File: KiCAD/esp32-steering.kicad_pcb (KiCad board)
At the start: 2 copper layers, 142 x 142 mm, 26 parts, among them J1 Conn_01x02, SW1 RotaryEncoder_Switch_MP, SW2 RotaryEncoder_Switch_MP, SW4 SW_SPST, SW5 SW_SPST

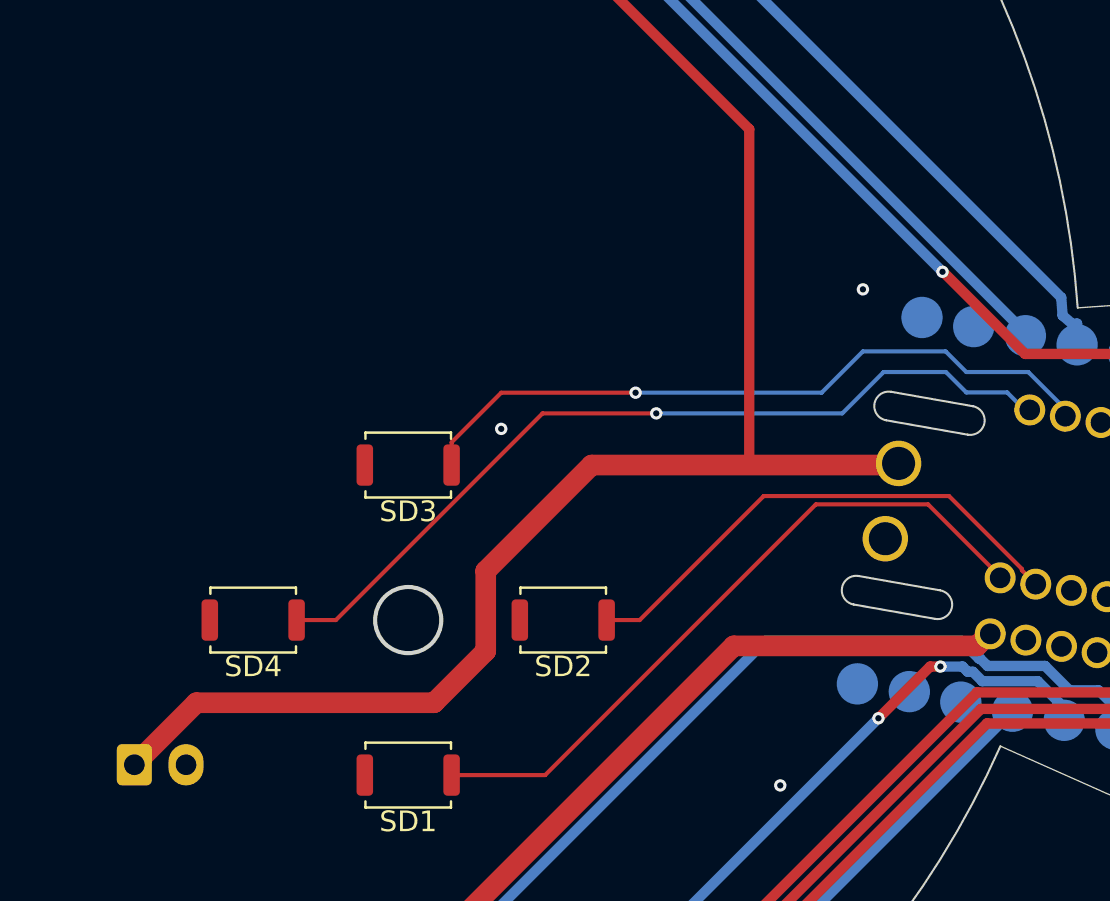
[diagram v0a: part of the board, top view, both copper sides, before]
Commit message: correct footprint and pcb design for battery connections
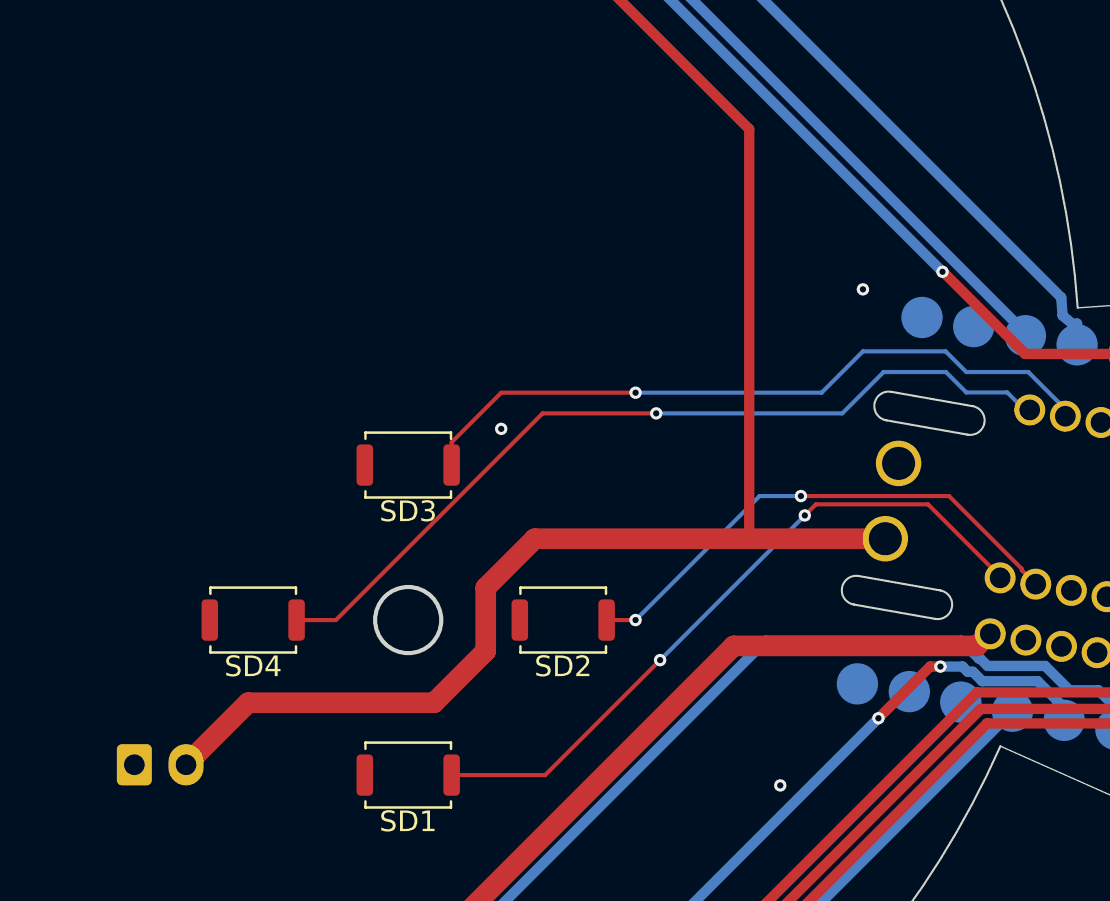
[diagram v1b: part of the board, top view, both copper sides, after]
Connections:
- J1 pad 1: +5V -> GND
- J1 pad 2: GND -> +5V
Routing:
- net +5V: track 169.2 -> 167.6 mm
- net /BUTD2: track 25.1 -> 25.3 mm, vias 0 -> 2
- net /BUTD1: vias 0 -> 2
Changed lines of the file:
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@@
 		(tags "D2FC-F-7N20M ")
 		(property "Reference" "SW5"
-			(at 0.040628 -12.709186 12.223)
+			(at 0.040629 -12.709186 12.223)
 			(unlocked yes)
 			(layer "B.SilkS")
@@
 			(remove_unused_layers no)
 			(roundrect_rratio 0.147059)
-			(net 25 "+5V")
+			(net 2 "GND")
 			(pinfunction "Pin_1")
 			(pintype "passive")
@@
 			(layers "*.Cu" "*.Mask")
 			(remove_unused_layers no)
-			(net 2 "GND")
+			(net 25 "+5V")
 			(pinfunction "Pin_2")
 			(pintype "passive")
@@
 		(fp_poly
 			(pts
-				(xy -4.5 13.25) (xy 4.500001 13.25) (xy 4.5 6.25) (xy -4.5 6.25)
+				(xy -4.5 13.25) (xy 4.500003 13.25) (xy 4.5 6.25) (xy -4.5 6.25)
 			)
 			(stroke
@@
 		(fp_arc
 			(start -5.2 7)
-			(mid -4.5 6.299999)
+			(mid -4.5 6.299998)
 			(end -3.8 7)
 			(stroke
@@
 		)
 		(pad "19" thru_hole circle
-			(at -1.85 10.05 260)
+			(at 1.85 10.05 260)
 			(size 2.2 2.2)
 			(drill 1.6)
@@
 		)
 		(pad "20" thru_hole circle
-			(at 1.85 10.05 260)
+			(at -1.85 10.05 260)
 			(size 2.2 2.2)
 			(drill 1.6)
@@
 	)
 	(segment
+		(start 135.725131 104.420742)
+		(end 135.645873 104.5)
+		(width 1)
+		(layer "F.Cu")
+		(net 2)
+	)
+	(segment
 		(start 160.351906 128.617429)
 		(end 160.351906 130.729669)
@@
 	)
 	(segment
-		(start 75.5 47)
-		(end 98.5 70)
+		(start 65.053238 44.370458)
+		(end 65.053238 47.37816)
 		(width 0.5)
 		(layer "F.Cu")
@@
 	)
 	(segment
-		(start 98.5 70)
-		(end 110.25 70)
+		(start 66.175078 48.5)
+		(end 67.75 48.5)
 		(width 0.5)
 		(layer "F.Cu")
@@
 	)
 	(segment
-		(start 135.725131 104.420742)
-		(end 135.645873 104.5)
-		(width 1)
+		(start 69.25 47)
+		(end 75.5 47)
+		(width 0.5)
 		(layer "F.Cu")
 		(net 25)
@@
 	)
 	(segment
-		(start 67.75 48.5)
-		(end 69.25 47)
+		(start 65.053238 47.37816)
+		(end 66.175078 48.5)
 		(width 0.5)
 		(layer "F.Cu")
@@
 	)
 	(segment
-		(start 135.645873 104.5)
-		(end 120.875 104.5)
-		(width 1)
+		(start 128.5 88.25)
+		(end 128.5 108.06453)
+		(width 0.5)
 		(layer "F.Cu")
 		(net 25)
 	)
 	(segment
-		(start 69.25 47)
-		(end 75.5 47)
+		(start 98.5 70)
+		(end 110.25 70)
 		(width 0.5)
 		(layer "F.Cu")
@@
 	)
 	(segment
+		(start 115.75 113.5)
+		(end 113.25 116)
+		(width 1)
+		(layer "F.Cu")
+		(net 25)
+	)
+	(segment
 		(start 130.703238 41.920458)
 		(end 130.703238 39.615617)
@@
 	)
 	(segment
-		(start 115.75 109.625)
-		(end 115.75 113.5)
+		(start 67.75 48.5)
+		(end 69.25 47)
+		(width 0.5)
+		(layer "F.Cu")
+		(net 25)
+	)
+	(segment
+		(start 118.12297 108.06453)
+		(end 115.75 110.4375)
 		(width 1)
 		(layer "F.Cu")
@@
 	)
 	(segment
-		(start 101.75 116)
-		(end 98.75 119)
-		(width 1)
-		(layer "F.Cu")
-		(net 25)
-	)
-	(segment
 		(start 93.736915 34.603531)
 		(end 93.736915 32.5)
@@
 	)
 	(segment
-		(start 115.75 113.5)
-		(end 113.25 116)
-		(width 1)
-		(layer "F.Cu")
-		(net 25)
-	)
-	(segment
-		(start 65.053238 44.370458)
-		(end 65.053238 47.37816)
-		(width 0.5)
-		(layer "F.Cu")
-		(net 25)
-	)
-	(segment
-		(start 128.5 88.25)
-		(end 128.5 104.25)
+		(start 75.5 47)
+		(end 98.5 70)
 		(width 0.5)
 		(layer "F.Cu")
@@
 	)
 	(segment
-		(start 65.053238 47.37816)
-		(end 66.175078 48.5)
-		(width 0.5)
-		(layer "F.Cu")
-		(net 25)
-	)
-	(segment
-		(start 113.25 116)
-		(end 101.75 116)
+		(start 135.082633 108.06453)
+		(end 118.12297 108.06453)
 		(width 1)
 		(layer "F.Cu")
@@
 	)
 	(segment
-		(start 71.747742 40.689522)
-		(end 71.747742 38.252258)
+		(start 110.25 70)
+		(end 128.5 88.25)
 		(width 0.5)
 		(layer "F.Cu")
@@
 	)
 	(segment
-		(start 128.5 104.25)
-		(end 128.75 104.5)
-		(width 0.5)
+		(start 104.25 116)
+		(end 101.25 119)
+		(width 1)
 		(layer "F.Cu")
 		(net 25)
 	)
 	(segment
-		(start 110.25 70)
-		(end 128.5 88.25)
-		(width 0.5)
+		(start 113.25 116)
+		(end 104.25 116)
+		(width 1)
 		(layer "F.Cu")
 		(net 25)
 	)
 	(segment
-		(start 66.175078 48.5)
-		(end 67.75 48.5)
+		(start 71.747742 40.689522)
+		(end 71.747742 38.252258)
 		(width 0.5)
 		(layer "F.Cu")
@@
 	)
 	(segment
-		(start 120.875 104.5)
-		(end 115.75 109.625)
+		(start 115.75 110.4375)
+		(end 115.75 113.5)
 		(width 1)
 		(layer "F.Cu")
@@
 	)
 	(segment
-		(start 131.724 106.401)
-		(end 137.151 106.401)
+		(start 140.638235 109.888235)
+		(end 140.638235 109.958017)
+		(width 0.2)
+		(layer "F.Cu")
+		(net 45)
+	)
+	(segment
+		(start 114.1 119.5)
+		(end 118.625 119.5)
 		(width 0.2)
 		(layer "F.Cu")
@@
 	)
 	(segment
-		(start 114.1 119.5)
-		(end 118.625 119.5)
+		(start 131.1875 106.9375)
+		(end 131.724 106.401)
 		(width 0.2)
 		(layer "F.Cu")
@@
 	)
 	(segment
-		(start 140.638235 109.888235)
-		(end 140.638235 109.958017)
+		(start 131.724 106.401)
+		(end 137.151 106.401)
 		(width 0.2)
 		(layer "F.Cu")
@@
 	(segment
 		(start 118.625 119.5)
-		(end 131.724 106.401)
+		(end 124.1875 113.9375)
 		(width 0.2)
 		(layer "F.Cu")
 		(net 45)
 	)
+	(via
+		(at 124.1875 113.9375)
+		(size 0.6)
+		(drill 0.3)
+		(layers "F.Cu" "B.Cu")
+		(net 45)
+	)
+	(via
+		(at 131.1875 106.9375)
+		(size 0.6)
+		(drill 0.3)
+		(layers "F.Cu" "B.Cu")
+		(net 45)
+	)
+	(segment
+		(start 131.1875 106.9375)
+		(end 124.1875 113.9375)
+		(width 0.2)
+		(layer "B.Cu")
+		(net 45)
+	)
 	(segment
 		(start 138.166557 106)
@@
 	(segment
 		(start 121.6 112)
-		(end 123.2 112)
+		(end 123 112)
 		(width 0.2)
 		(layer "F.Cu")
@@
 	)
 	(segment
-		(start 141.689235 109.589488)
-		(end 142.361648 110.261901)
+		(start 131 106)
+		(end 138.166557 106)
 		(width 0.2)
 		(layer "F.Cu")
@@
 	)
 	(segment
-		(start 129.2 106)
-		(end 138.166557 106)
+		(start 141.689235 109.589488)
+		(end 142.361648 110.261901)
 		(width 0.2)
 		(layer "F.Cu")
@@
 	)
 	(segment
-		(start 123.2 112)
-		(end 129.2 106)
+		(start 123 112)
+		(end 123.2 112)
 		(width 0.2)
 		(layer "F.Cu")
 		(net 46)
 	)
+	(via
+		(at 131 106)
+		(size 0.6)
+		(drill 0.3)
+		(layers "F.Cu" "B.Cu")
+		(net 46)
+	)
+	(via
+		(at 123 112)
+		(size 0.6)
+		(drill 0.3)
+		(layers "F.Cu" "B.Cu")
+		(net 46)
+	)
+	(segment
+		(start 131 106)
+		(end 129 106)
+		(width 0.2)
+		(layer "B.Cu")
+		(net 46)
+	)
+	(segment
+		(start 129 106)
+		(end 123 112)
+		(width 0.2)
+		(layer "B.Cu")
+		(net 46)
+	)
